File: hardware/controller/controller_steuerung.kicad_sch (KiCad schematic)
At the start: 68 parts, among them J3 DISPLAY, J4 PANEL, J5 TC top, J6 TC bot, J7 USB-C, J9 UART, Q6 AO3401A, Q7 IRLML6346, SW1 RESET, SW2 BOOT, U10 USBLC6-2SC6, U11 USBLC6-2SC6, U12 USBLC6-2SC6, U3 ESP32-S3-WROOM-1U-N8, U4 USBLC6-2SC6, U5 MAX31856MUD+, U6 MAX31856MUD+

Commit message: feat(hardware): board fan circuit in the schematic (T073), sheet cleanup in progress
Fan header J10 with BSS138 PWM stage (GPIO 38, 1k pull-up to 5 V,
full speed without firmware) and tachometer input (GPIO 37, 10k/1k/1n,
TP12) per research R18. Reference netlist re-exported for this
deliberate change: 129 parts, 73 nets. board_rev_a.h and
check_schematic.py know FAN_TACH/FAN_PWM. PCB updated from the netlist,
new footprints parked below the outline; parity DRC clean.
Includes the user's partial sheet cleanup (T071 still open).

Co-Authored-By: Claude Opus 5.5 <noreply@anthropic.com>
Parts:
- added C31: 10u, Capacitor_SMD:C_0805_2012Metric, symbol Device:C
- added C32: 100n, Capacitor_SMD:C_0603_1608Metric, symbol Device:C
- added C33: 1n, Capacitor_SMD:C_0603_1608Metric, symbol Device:C
- added J10: FAN, Connector:FanPinHeader_1x04_P2.54mm_Vertical, symbol Connector_Generic:Conn_01x04
- added Q8: BSS138, Package_TO_SOT_SMD:SOT-23, symbol Transistor_FET:AO3400A
- added R40: 100k, Resistor_SMD:R_0603_1608Metric, symbol Device:R
- added R41, R43: 1k, Resistor_SMD:R_0603_1608Metric, symbol Device:R
- added R42: 10k, Resistor_SMD:R_0603_1608Metric, symbol Device:R
- added TP12: FAN_TACH, TestPoint:TestPoint_Keystone_5000-5004_Miniature, symbol Connector:TestPoint
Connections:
- net +3V3: now also R42.1
- net +5V: now also C31.1, C32.1, J10.2 (Pin_2), R41.1
- net GND: now also C31.2, C32.2, C33.2, J10.1 (Pin_1), Q8.2 (S), R40.2
- net FAN_TACH: now reaches U3.30 (IO37)
- net FAN_TACH: now also C33.1, R43.2, TP12.1
- net FAN_PWM: now reaches U3.31 (IO38)
- net FAN_PWM: now also Q8.1 (G), R40.1
- new net FAN_PWM_5V: J10.4 (Pin_4), Q8.3 (D), R41.2
- new net FAN_TACH_RAW: J10.3 (Pin_3), R42.2, R43.1
- no-connect marks 12 -> 10
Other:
- note added: "Lüfter"
- note added: "Noctua NF-A4x10 5V PWM in der Gehäusewand (research R18). PWM 25 kHz invertiert über Q8; ohne Firmware sperrt Q8 und der Lüfter läuft mit voller Drehzahl. Drehzahl: Open Collector, 2 Pulse je Umdrehung, Zählung per PCNT."
- moved on the sheet: C11, C17, R8, R9, U4

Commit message: feat(hardware): sheet cleanup done, ERC clean (T071)
- Leistung/Steuerung sheets cleaned up and readable, intersheet references on
- embedded symbols updated from the libraries (lib_symbol_mismatch gone)
- stray and off-grid wire stubs removed
- PWR_FLAGs on N_IN, L_FUSED, +5V and VBUS
- ERC exclusion for the shared SDO line of U5/U6 (MAX31856, tristate)
- PCB nets re-imported, U7 relinked

kicad-cli ERC: 0 violations, check_schematic: 0 errors, parity DRC clean.

Co-Authored-By: Claude Opus 5.5 <noreply@anthropic.com>
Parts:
- added R16: 220, Resistor_SMD:R_0603_1608Metric, symbol Device:R
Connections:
- net +3V3: now also R16.1
- net ENC_A_RAW: no longer names the net of J4.1 (Pin_1), R30.2, R31.1, U10.1 (I/O1), U10.6 (I/O1)
- net ENC_B_RAW: no longer names the net of J4.3 (Pin_3), R32.2, R33.1, U10.3 (I/O2), U10.4 (I/O2)
- net ENC_SW_RAW: no longer names the net of J4.4 (Pin_4), R34.2, R35.1, U11.1 (I/O1), U11.6 (I/O1)
- net STOP_NC_OUT: no longer names the net of J4.5 (Pin_5), U12.1 (I/O1), U12.6 (I/O1)
- net STOP_NC_OUT: now also R16.2
- net STOP_NO_RAW: no longer names the net of J4.7 (Pin_7), R36.2, R37.1, U11.3 (I/O2), U11.4 (I/O2)
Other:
- moved on the sheet: C14, C17, C27, C28, C29, C30, C31, C32, C33, J10, J5, J6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

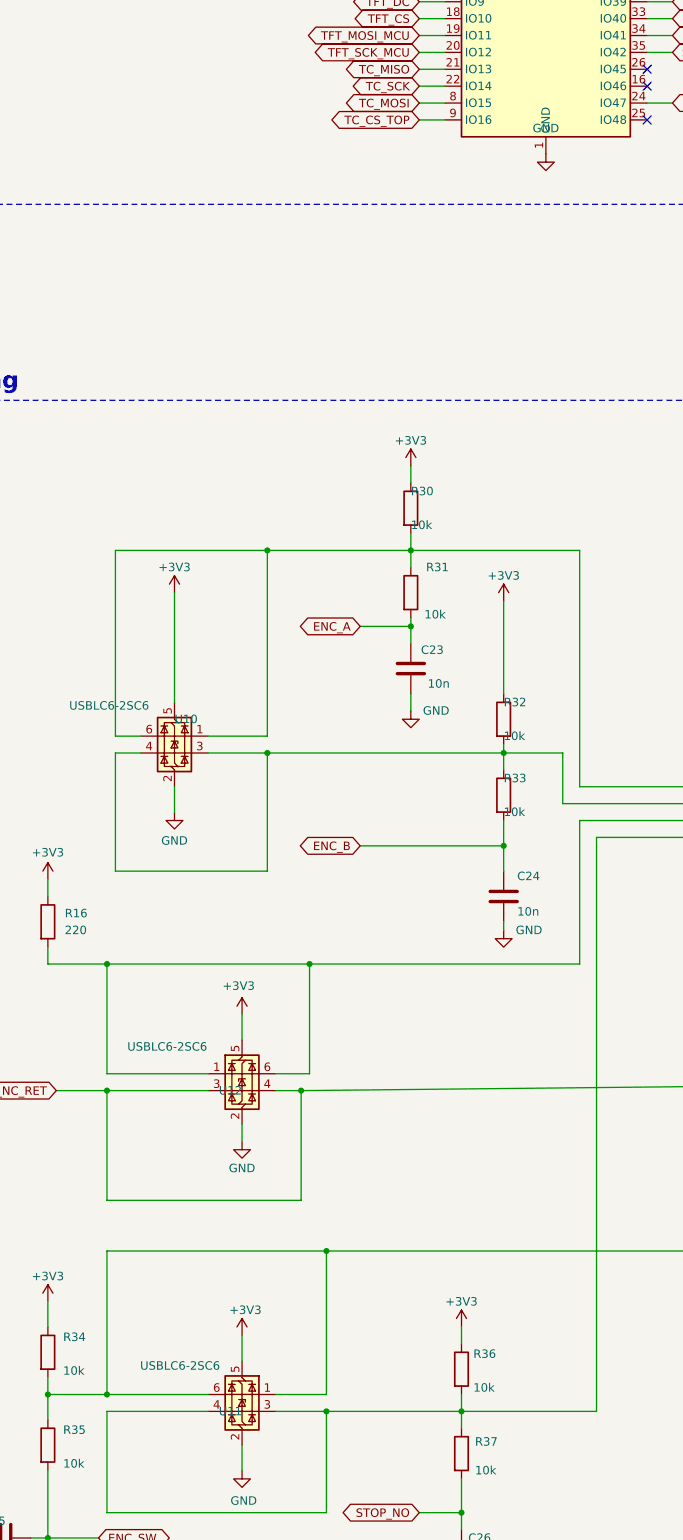
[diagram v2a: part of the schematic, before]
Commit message: feat(hardware): thermocouple sockets J5/J6 switched to RS PRO 381-7564
- Omega PCC-SMP-K (46 EUR per 5-pack, dimensions only from an isometric
  drawing) replaced by RS PRO 381-7564 (type K IEC, NiCr/Ni contacts,
  about 5 EUR each, dimensioned drawing in the RS datasheet)
- new footprint oven:RS_381-7564_Horizontal: 2 pins at 7.9 mm, NPTH 2.7 mm
  for an M2.5 screw; polarity still to be checked on a sample
- schematic fields footprint/MPN/source, controller.ref.net re-exported
  (intended change; it also takes over the net names after the label
  cleanup, connectivity unchanged)
- J5/J6 swapped on the board, pins below U5/U6, 2.7 mm gap between them
- small part placement optimised for routing, silkscreen cleaned up (T020)
- value texts at U1/RV1 moved (user)
- docs and BOM updated, old Omega footprint removed

check_schematic: 0 errors, 0 notes; DRC with schematic parity: no
deviation, only unconnected items and 2 silk edge warnings at U1.

Co-Authored-By: Claude Opus 5.5 <noreply@anthropic.com>
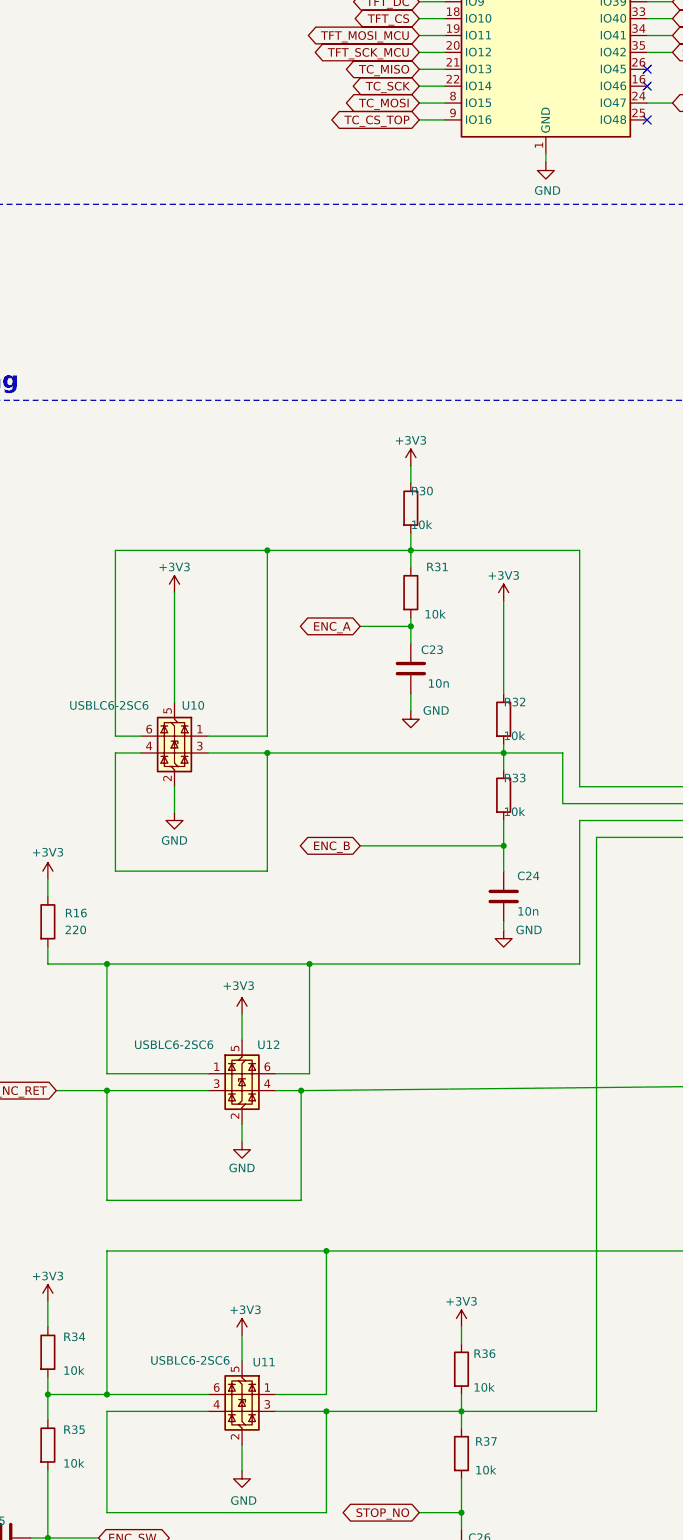
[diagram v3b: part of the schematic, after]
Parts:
- J5, J6: footprint oven:Omega_PCC-SMP_Horizontal -> oven:RS_381-7564_Horizontal; MPN Omega PCC-SMP-K -> RS PRO 381-7564; Source Farnell 3794917 -> RS 381-7564
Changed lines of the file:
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@@
 	(wire
 		(pts
+			(xy 125.73 137.16) (xy 125.73 135.89)
+		)
+		(stroke
+			(width 0)
+			(type default)
+		)
+	)
+	(wire
+		(pts
 			(xy 59.69 92.71) (xy 110.49 92.71)
 		)
@@
 			)
 		)
-		(property "Footprint" "oven:Omega_PCC-SMP_Horizontal"
+		(property "Footprint" "oven:RS_381-7564_Horizontal"
 			(at 372.11 124.46 90)
 			(hide yes)
@@
 			)
 		)
-		(property "MPN" "Omega PCC-SMP-K"
+		(property "MPN" "RS PRO 381-7564"
 			(at 367.03 124.46 90)
 			(hide yes)
@@
 			)
 		)
-		(property "Source" "Farnell 3794917"
+		(property "Source" "RS 381-7564"
 			(at 365.76 124.46 90)
 			(hide yes)
@@
 		(dnp no)
 		(property "Reference" "U12"
-			(at 80.01 276.86 180)
+			(at 82.296 270.002 0)
 			(show_name no)
 			(do_not_autoplace no)
@@
 		)
 		(property "Value" "USBLC6-2SC6"
-			(at 62.738 270.256 0)
+			(at 63.754 270.002 0)
 			(show_name no)
 			(do_not_autoplace no)
@@
 		(dnp no)
 		(property "Reference" "U10"
-			(at 69.85 220.98 180)
+			(at 74.422 218.948 0)
 			(show_name no)
 			(do_not_autoplace no)
@@
 		(dnp no)
 		(property "Reference" "U11"
-			(at 80.01 325.12 0)
+			(at 85.09 317.754 0)
 			(show_name no)
 			(do_not_autoplace no)
@@
 		)
 		(property "Value" "USBLC6-2SC6"
-			(at 76.708 318.262 0)
+			(at 78.232 317.5 0)
 			(show_name no)
 			(do_not_autoplace no)
@@
 	(symbol
 		(lib_id "power:GND")
-		(at 125.73 135.89 0)
+		(at 125.73 137.16 0)
 		(unit 1)
 		(body_style 1)
@@
 		(in_pos_files yes)
 		(dnp no)
-		(fields_autoplaced yes)
 		(property "Reference" "#PWR060"
-			(at 125.73 134.62 0)
+			(at 125.73 135.89 0)
 			(hide yes)
 			(show_name no)
@@
 		)
 		(property "Value" "GND"
-			(at 125.73 132.08 0)
+			(at 125.984 141.478 0)
 			(show_name no)
 			(do_not_autoplace no)
@@
 		)
 		(property "Footprint" ""
-			(at 125.73 135.89 0)
+			(at 125.73 137.16 0)
 			(hide yes)
 			(show_name no)
@@
 		)
 		(property "Datasheet" ""
-			(at 125.73 135.89 0)
+			(at 125.73 137.16 0)
 			(hide yes)
 			(show_name no)
@@
 		)
 		(property "Description" ""
-			(at 125.73 135.89 0)
+			(at 125.73 137.16 0)
 			(show_name no)
 			(do_not_autoplace no)
@@
 			)
 		)
-		(property "Footprint" "oven:Omega_PCC-SMP_Horizontal"
+		(property "Footprint" "oven:RS_381-7564_Horizontal"
 			(at 461.01 123.19 90)
 			(hide yes)
@@
 			)
 		)
-		(property "MPN" "Omega PCC-SMP-K"
+		(property "MPN" "RS PRO 381-7564"
 			(at 455.93 123.19 90)
 			(hide yes)
@@
 			)
 		)
-		(property "Source" "Farnell 3794917"
+		(property "Source" "RS 381-7564"
 			(at 454.66 123.19 90)
 			(hide yes)
